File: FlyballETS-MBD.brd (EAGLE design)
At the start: 53.3 x 63.5 mm, 16 parts, among them Q1 BC557, Q2 BC557

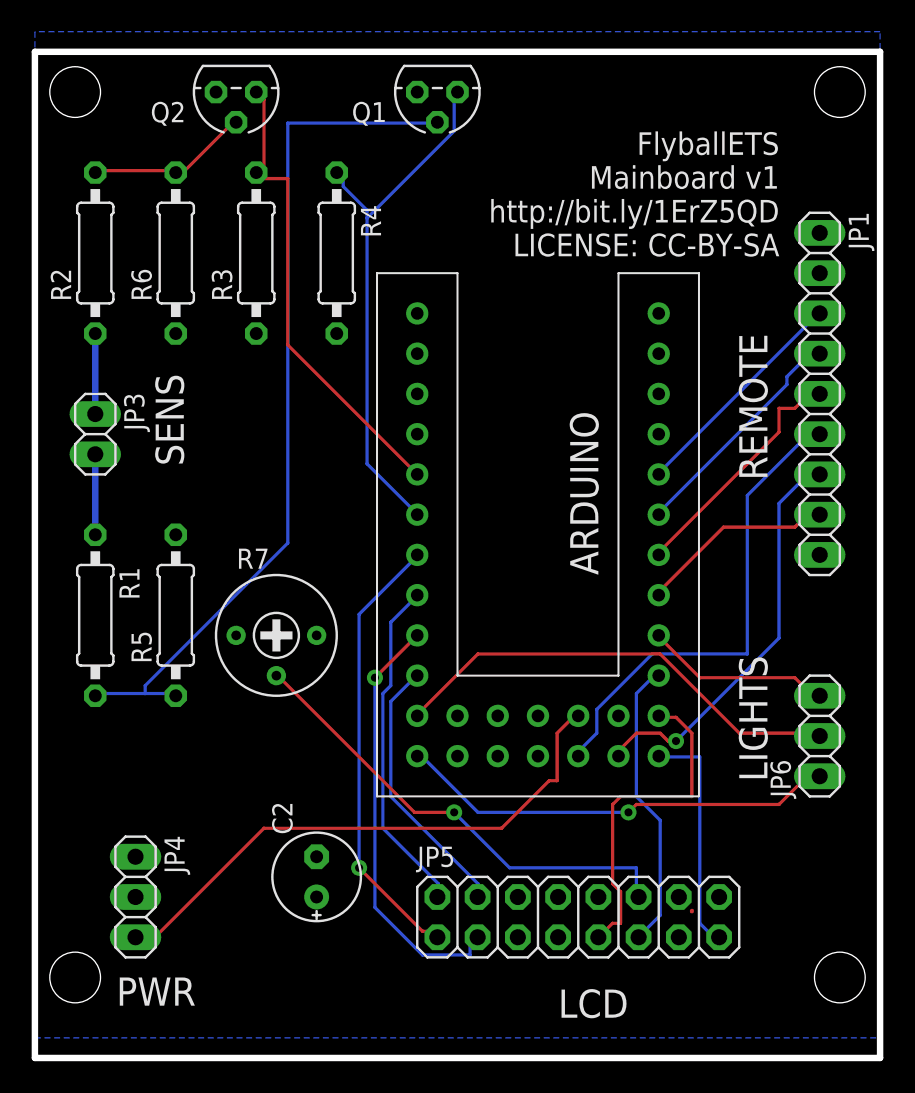
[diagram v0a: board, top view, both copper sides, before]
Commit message: Updated drawings and added PNG exports
- Added frames around drawings to make it look neater
- Added PNG export files so people who don't have EAGLE can see
everything
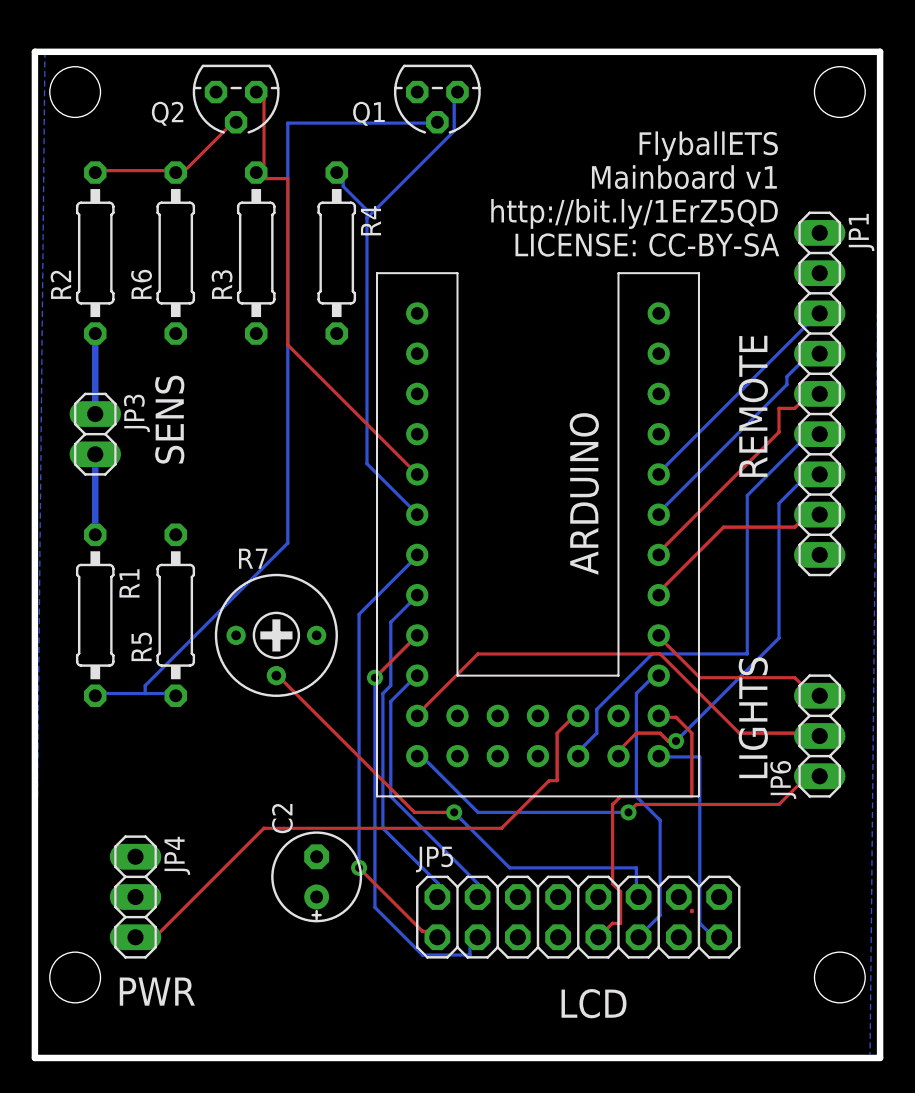
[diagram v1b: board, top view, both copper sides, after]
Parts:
- added U$1: (no value), frames:A5L-LOC
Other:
- board text added: "Alex Goris"
- board text added: "Units: mm"
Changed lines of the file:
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@@
 http://bit.ly/1ErZ5QD
 LICENSE: CC-BY-SA</text>
+<text x="22.86" y="-30.48" size="2.54" layer="48">FlyballETS
+Mainboard v1
+http://bit.ly/1ErZ5QD
+LICENSE: CC-BY-SA</text>
+<text x="74.93" y="-17.78" size="2.54" layer="48">Alex Goris</text>
+<dimension x1="55.88" y1="0" x2="55.88" y2="63.5" x3="63.5" y3="31.75" textsize="2.54" layer="48"/>
+<dimension x1="2.54" y1="63.5" x2="55.88" y2="63.5" x3="29.21" y3="68.58" textsize="2.54" layer="48"/>
+<text x="74.93" y="-33.02" size="2.54" layer="48">Units: mm</text>
 </plain>
 <attributes>
@@
 <element name="C2" library="resistor" package="E2,5-6E" value="100nF" x="20.32" y="11.43" rot="R90"/>
 <element name="U$2" library="_custom" package="ARDPROMINISOCK" value="ARDPROMINISOCK" x="44.45" y="49.53" rot="R180"/>
+<element name="U$1" library="frames" package="A5L-LOC" value="" x="-66.04" y="-38.1"/>
 </elements>
 <signals>
@@
 <contactref element="U$2" pad="GND@3"/>
 <polygon width="0.4064" layer="16">
-<vertex x="2.54" y="1.27"/>
-<vertex x="55.88" y="1.27"/>
-<vertex x="55.88" y="64.77"/>
-<vertex x="2.54" y="64.77"/>
+<vertex x="2.54" y="0"/>
+<vertex x="55.245" y="0"/>
+<vertex x="55.88" y="63.5"/>
+<vertex x="3.175" y="63.5"/>
 </polygon>
 </signal>

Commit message: Mainboard v2
- Changed connectors to use JST-XH type
- For LCD screen use flatcable/ribboncable connector (2x9 pins)
- Repositioned everything to allow for smaller board size (12% smaller)
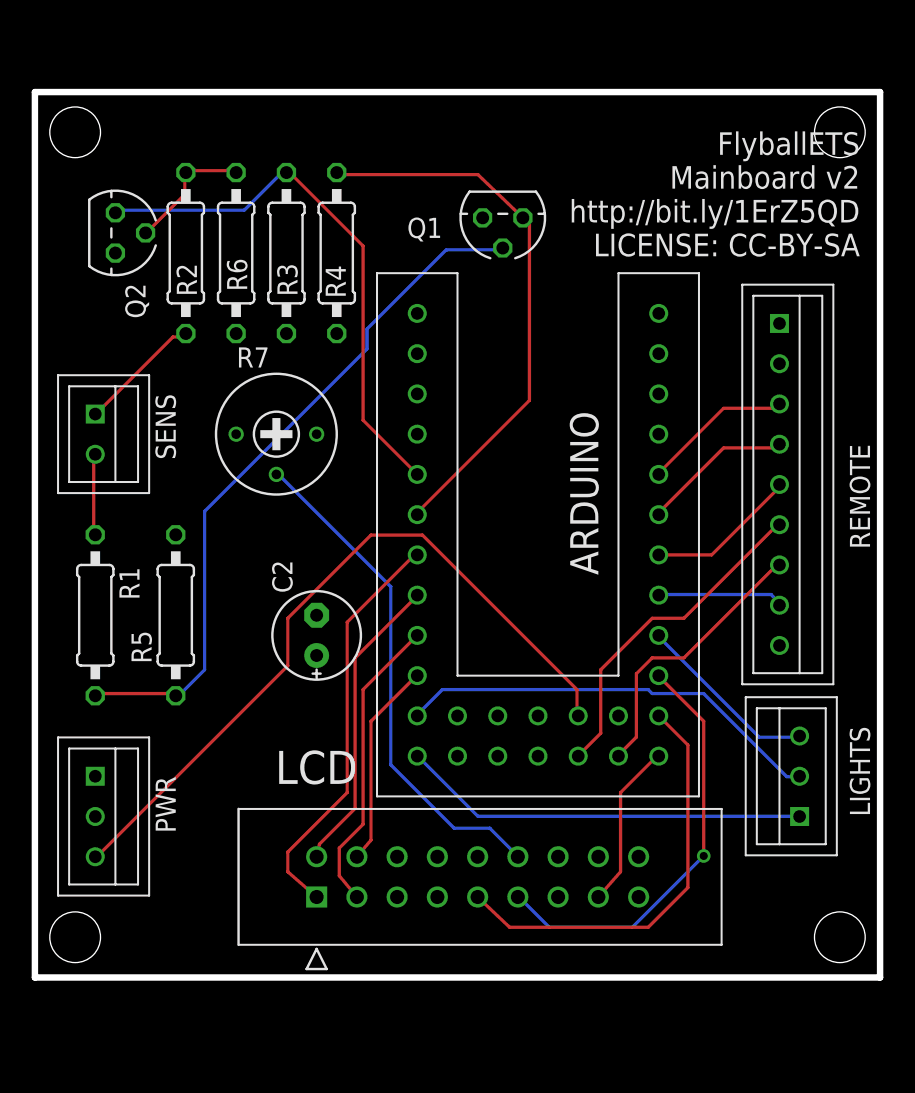
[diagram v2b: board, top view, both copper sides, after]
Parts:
- removed JP1: (no value), pinhead:1X09
- removed JP3: (no value), pinhead:1X02
- removed JP4, JP6: (no value), pinhead:1X03
- removed JP5: (no value), pinhead:2X08
- added LCD: 2518-6002UB, 3M_By_element14_Batch_1:3M_2518-6002UB
- added LIGHTS, PWR: 03-JST-B3B-XH-A, bt_con-jst-xh:B3B-XH
- added REMOTE: 09-JST, bt_con-jst-xh:B9B-XH
- added SENS: 02-JST, bt_con-jst-xh:B2B-XH
- moved C2 15.2 mm to (20.3, 26.7)
- moved R7 12.7 mm to (17.8, 39.4)
- moved Q2 11.7 mm to (7.62, 52.1), turned to 270 degrees
- moved Q1 8.95 mm to (32.1, 53.0)
- moved R2 5.71 mm to (12.1, 50.8)
- moved R6 3.81 mm to (15.2, 50.8)
- moved R3 1.90 mm to (18.4, 50.8)
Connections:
- net +5V: now also LCD.14, LCD.17, PWR.P$2, REMOTE.P$1; no longer JP1.1, JP4.2, JP5.14
- net CLK: now also LIGHTS.P$2; no longer JP6.2
- net D0: now also REMOTE.P$3; no longer JP1.3
- net D1: now also REMOTE.P$4; no longer JP1.4
- net D2: now also REMOTE.P$5; no longer JP1.5
- net D3: now also REMOTE.P$6; no longer JP1.6
- net D4: now also REMOTE.P$7; no longer JP1.7
- net D5: now also REMOTE.P$8; no longer JP1.8
- net DATA: now also LIGHTS.P$1; no longer JP6.1
- net DB4: now also LCD.4; no longer JP5.4
- net DB5: now also LCD.3; no longer JP5.3
- net DB6: now also LCD.2; no longer JP5.2
- net DB7: now also LCD.1; no longer JP5.1
- net E1: now also LCD.9; no longer JP5.9
- net E2: now also LCD.15; no longer JP5.15
- net GND: now also LCD.10, LCD.13, LCD.18, PWR.P$1, REMOTE.P$2; no longer JP1.2, JP4.1, JP5.10, JP5.13
- net N$1: now also SENS.P$2; no longer JP3.2
- net N$2: now also SENS.P$1; no longer JP3.1
- net N$5: now also LCD.12; no longer JP5.12
- net RCLK: now also LIGHTS.P$3; no longer JP6.3
- net RS: now also LCD.11; no longer JP5.11
- net VSENS: now also PWR.P$3; no longer JP4.3
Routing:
- net VSENS: track 35.6 -> 46.3 mm
- net N$3: track 54.3 -> 44.2 mm
- net D3: track 30.7 -> 21.2 mm
- net RS: track 18.4 -> 26.9 mm, vias 0 -> 1
- net DB5: track 27.0 -> 18.9 mm, vias 1 -> 0
- net D4: track 25.7 -> 17.7 mm, vias 1 -> 0
- net D2: track 15.5 -> 9.55 mm
- net E1: track 21.2 -> 26.7 mm
- net D1: track 14.9 -> 9.62 mm
- net D0: track 14.4 -> 9.49 mm
- net S1: track 29.9 -> 34.6 mm
- net D5: track 12.5 -> 7.98 mm
- net E2: track 14.8 -> 10.5 mm
- net DB4: track 17.0 -> 13.0 mm
- net N$2: track 5.08 -> 7.88 mm
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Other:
- board size 53.3 x 63.5 mm -> 53.3 x 55.9 mm
- board text added: "FlyballETS Mainboard v2 http://bit.ly/1ErZ5QD LICENSE: CC-BY-SA"
- board text removed: "FlyballETS Mainboard v1 http://bit.ly/1ErZ5QD LICENSE: CC-BY-SA"
- board text removed: "LCD"
- board text removed: "LIGHTS"
- board text removed: "PWR"
- board text removed: "REMOTE"
- board text removed: "SENS"

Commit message: Minor updates + added BOMs
- Updated to EAGLE 7.5.0
- Added BOM text file exports
- Renamed arduino socket on MBD board
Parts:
- renumbered U$2 to ARDUINO
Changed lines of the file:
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@@
 <?xml version="1.0" encoding="utf-8"?>
 <!DOCTYPE eagle SYSTEM "eagle.dtd">
-<eagle version="7.4.0">
+<eagle version="7.5.0">
 <drawing>
 <settings>
@@
 <element name="Q2" library="transistor-pnp" package="TO92" value="BC557" x="7.62" y="52.07" rot="R270"/>
 <element name="C2" library="resistor" package="E2,5-6E" value="100nF" x="20.32" y="26.67" rot="R90"/>
-<element name="U$2" library="_custom" package="ARDPROMINISOCK" value="ARDPROMINISOCK" x="44.45" y="49.53" smashed="yes" rot="R180"/>
+<element name="ARDUINO" library="_custom" package="ARDPROMINISOCK" value="ARDPROMINISOCK" x="44.45" y="49.53" smashed="yes" rot="R180"/>
 <element name="U$1" library="frames" package="A5L-LOC" value="" x="-66.04" y="-38.1"/>
 <element name="LCD" library="3M_By_element14_Batch_1" package="3M_2518-6002UB" value="2518-6002UB" x="20.32" y="12.7" smashed="yes" rot="R180">
@@
 <contactref element="R7" pad="1"/>
 <contactref element="C2" pad="-"/>
-<contactref element="U$2" pad="GND@3"/>
+<contactref element="ARDUINO" pad="GND@3"/>
 <contactref element="LCD" pad="10"/>
 <contactref element="LCD" pad="13"/>
@@
 </signal>
 <signal name="D0">
-<contactref element="U$2" pad="A3"/>
+<contactref element="ARDUINO" pad="A3"/>
 <contactref element="REMOTE" pad="P$3"/>
 <wire x1="46" y1="41" x2="42" y2="37" width="0.2032" layer="1"/>
@@
 <contactref element="Q2" pad="1"/>
 <contactref element="C2" pad="+"/>
-<contactref element="U$2" pad="VCC@1"/>
+<contactref element="ARDUINO" pad="VCC@1"/>
 <polygon width="0.4064" layer="1">
 <vertex x="2.54" y="5.08"/>
@@
 </signal>
 <signal name="D1">
-<contactref element="U$2" pad="A2"/>
+<contactref element="ARDUINO" pad="A2"/>
 <contactref element="REMOTE" pad="P$4"/>
 <wire x1="46" y1="38.5" x2="42" y2="34.5" width="0.2032" layer="1"/>
@@
 </signal>
 <signal name="D2">
-<contactref element="U$2" pad="A1"/>
+<contactref element="ARDUINO" pad="A1"/>
 <contactref element="REMOTE" pad="P$5"/>
 <wire x1="45.25" y1="31.75" x2="41.91" y2="31.75" width="0.2032" layer="1"/>
@@
 </signal>
 <signal name="D3">
-<contactref element="U$2" pad="A4"/>
+<contactref element="ARDUINO" pad="A4"/>
 <contactref element="REMOTE" pad="P$6"/>
 <wire x1="38.25" y1="20.5" x2="37" y2="19.25" width="0.2032" layer="1"/>
@@
 </signal>
 <signal name="D4">
-<contactref element="U$2" pad="A5"/>
+<contactref element="ARDUINO" pad="A5"/>
 <contactref element="REMOTE" pad="P$7"/>
 <wire x1="40.5" y1="20.25" x2="39.5" y2="19.25" width="0.2032" layer="1"/>
@@
 </signal>
 <signal name="D5">
-<contactref element="U$2" pad="A0"/>
+<contactref element="ARDUINO" pad="A0"/>
 <contactref element="REMOTE" pad="P$8"/>
 <wire x1="49" y1="29.25" x2="42" y2="29.25" width="0.2032" layer="16"/>
@@
 </signal>
 <signal name="E1">
-<contactref element="U$2" pad="11"/>
+<contactref element="ARDUINO" pad="11"/>
 <contactref element="LCD" pad="9"/>
 <wire x1="43.75" y1="19.75" x2="41.91" y2="21.59" width="0.2032" layer="1"/>
@@
 </signal>
 <signal name="RS">
-<contactref element="U$2" pad="12"/>
+<contactref element="ARDUINO" pad="12"/>
 <contactref element="LCD" pad="11"/>
 <wire x1="44.75" y1="21.25" x2="42" y2="24" width="0.2032" layer="1"/>
@@
 </signal>
 <signal name="E2">
-<contactref element="U$2" pad="10"/>
+<contactref element="ARDUINO" pad="10"/>
 <contactref element="LCD" pad="15"/>
 <wire x1="39.5" y1="16.75" x2="41.75" y2="19" width="0.2032" layer="1"/>
@@
 </signal>
 <signal name="DATA">
-<contactref element="U$2" pad="9"/>
+<contactref element="ARDUINO" pad="9"/>
 <contactref element="LIGHTS" pad="P$1"/>
 <wire x1="30.5" y1="15.25" x2="26.75" y2="19" width="0.2032" layer="16"/>
@@
 </signal>
 <signal name="CLK">
-<contactref element="U$2" pad="8"/>
+<contactref element="ARDUINO" pad="8"/>
 <contactref element="LIGHTS" pad="P$2"/>
 <wire x1="28.25" y1="23.25" x2="26.75" y2="21.75" width="0.2032" layer="16"/>
@@
 </signal>
 <signal name="RCLK">
-<contactref element="U$2" pad="13"/>
+<contactref element="ARDUINO" pad="13"/>
 <contactref element="LIGHTS" pad="P$3"/>
 <wire x1="48.25" y1="20.25" x2="42" y2="26.5" width="0.2032" layer="16"/>
@@
 <contactref element="Q1" pad="3"/>
 <contactref element="R4" pad="1"/>
-<contactref element="U$2" pad="3"/>
+<contactref element="ARDUINO" pad="3"/>
 <wire x1="33.75" y1="41.5" x2="26.75" y2="34.5" width="0.2032" layer="1"/>
 <wire x1="33.75" y1="52.75" x2="33.75" y2="41.5" width="0.2032" layer="1"/>
@@
 <contactref element="R3" pad="2"/>
 <contactref element="Q2" pad="3"/>
-<contactref element="U$2" pad="2"/>
+<contactref element="ARDUINO" pad="2"/>
 <wire x1="23.25" y1="40.25" x2="26.67" y2="36.83" width="0.2032" layer="1"/>
 <wire x1="23.25" y1="51.25" x2="23.25" y2="40.25" width="0.2032" layer="1"/>
@@
 </signal>
 <signal name="DB7">
-<contactref element="U$2" pad="4"/>
+<contactref element="ARDUINO" pad="4"/>
 <contactref element="LCD" pad="1"/>
 <wire x1="22.25" y1="27.5" x2="26.5" y2="31.75" width="0.2032" layer="1"/>
@@
 </signal>
 <signal name="DB5">
-<contactref element="U$2" pad="6"/>
+<contactref element="ARDUINO" pad="6"/>
 <contactref element="LCD" pad="3"/>
 <wire x1="23.25" y1="23.25" x2="26.67" y2="26.67" width="0.2032" layer="1"/>
@@
 </signal>
 <signal name="DB6">
-<contactref element="U$2" pad="5"/>
+<contactref element="ARDUINO" pad="5"/>
 <contactref element="LCD" pad="2"/>
 <wire x1="22.75" y1="25.25" x2="26.5" y2="29" width="0.2032" layer="1"/>
@@
 </signal>
 <signal name="DB4">
-<contactref element="U$2" pad="7"/>
+<contactref element="ARDUINO" pad="7"/>
 <contactref element="LCD" pad="4"/>
 <wire x1="23.75" y1="21.25" x2="26.5" y2="24" width="0.2032" layer="1"/>
@@
 </signal>
 <signal name="VSENS">
-<contactref element="U$2" pad="A6"/>
+<contactref element="ARDUINO" pad="A6"/>
 <contactref element="PWR" pad="P$3"/>
 <wire x1="18.5" y1="24.75" x2="6.5" y2="12.75" width="0.2032" layer="1"/>

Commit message: Incorrect capacitor value
Changed 100nF to 100uF
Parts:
- C2: value 100nF -> 100uF
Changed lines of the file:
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@@
 <element name="R7" library="resistor" package="RTRIM3339P" value="10k" x="17.78" y="39.37"/>
 <element name="Q2" library="transistor-pnp" package="TO92" value="BC557" x="7.62" y="52.07" rot="R270"/>
-<element name="C2" library="resistor" package="E2,5-6E" value="100nF" x="20.32" y="26.67" rot="R90"/>
+<element name="C2" library="resistor" package="E2,5-6E" value="100uF" x="20.32" y="26.67" rot="R90"/>
 <element name="ARDUINO" library="_custom" package="ARDPROMINISOCK" value="ARDPROMINISOCK" x="44.45" y="49.53" smashed="yes" rot="R180"/>
 <element name="U$1" library="frames" package="A5L-LOC" value="" x="-66.04" y="-38.1"/>
